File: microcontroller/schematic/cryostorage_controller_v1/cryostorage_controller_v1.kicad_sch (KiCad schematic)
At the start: 27 parts, among them J1 Screw_Terminal_01x04, J2 USB_A_Stacked, J3 Screw_Terminal_01x06, J4 Screw_Terminal_01x06, J5 Screw_Terminal_01x05, J6 Screw_Terminal_01x01, J7 Screw_Terminal_01x02, Q1 IRLB8721PBF, Q2 BSS138, Q3 IRLB8721PBF, Q4 IRLB8721PBF, Q5 BSS138, U1 Pico, U2 LT1086-3.3

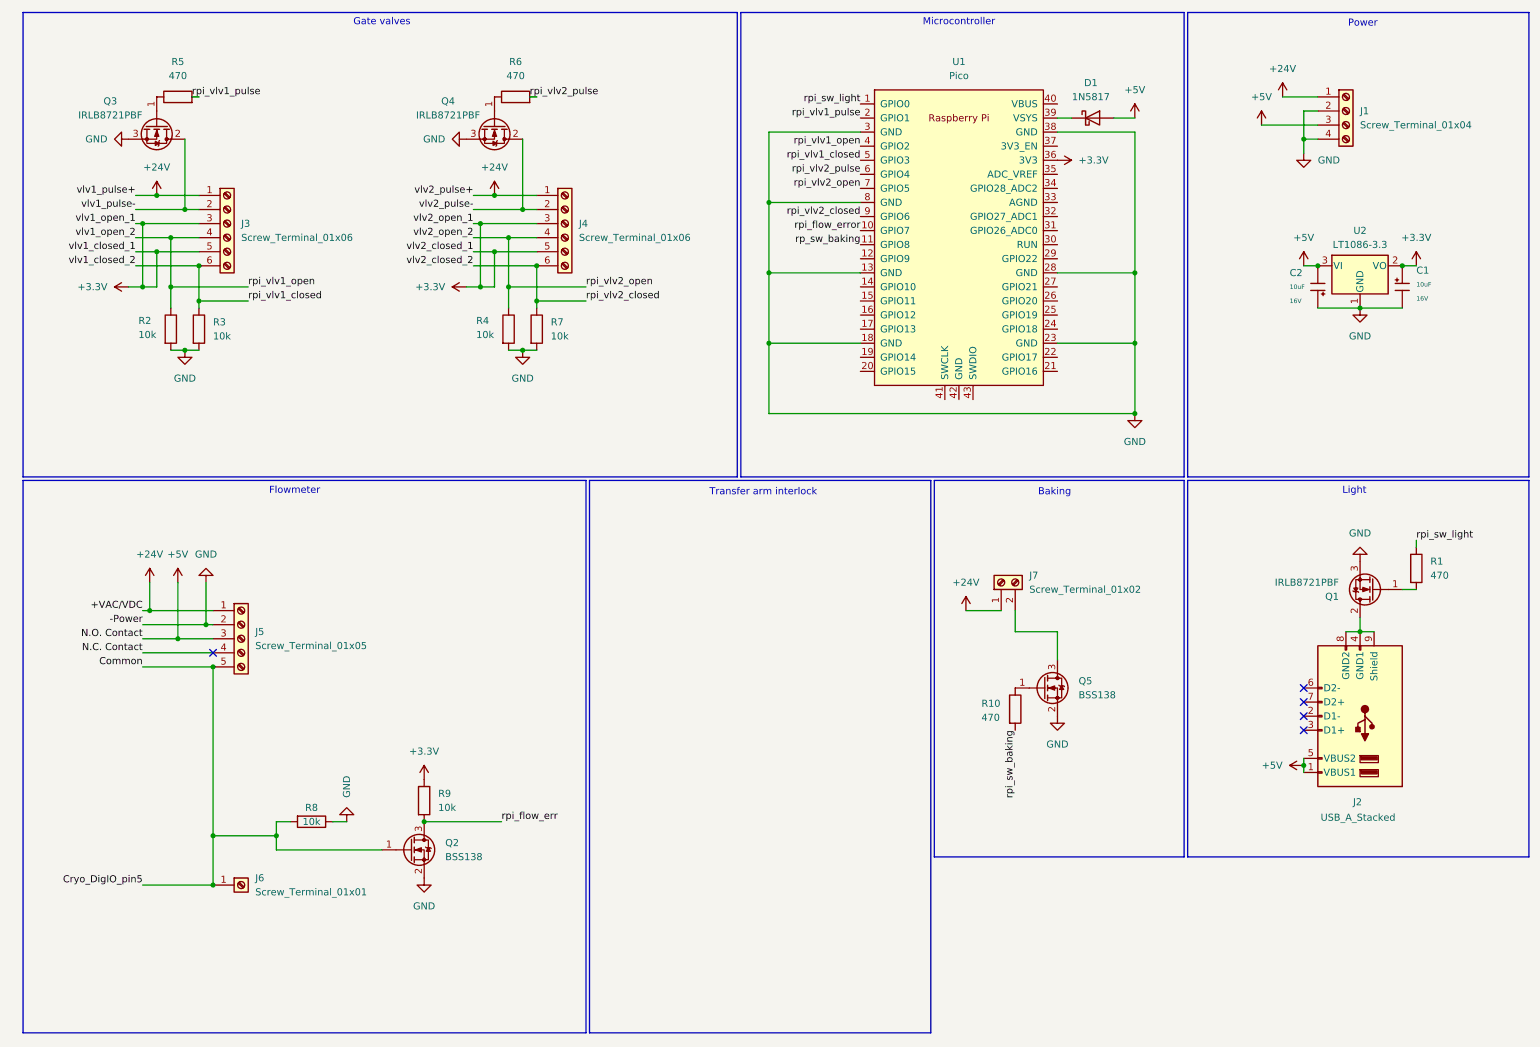
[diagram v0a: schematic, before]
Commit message: update schematic and add first PCB final version
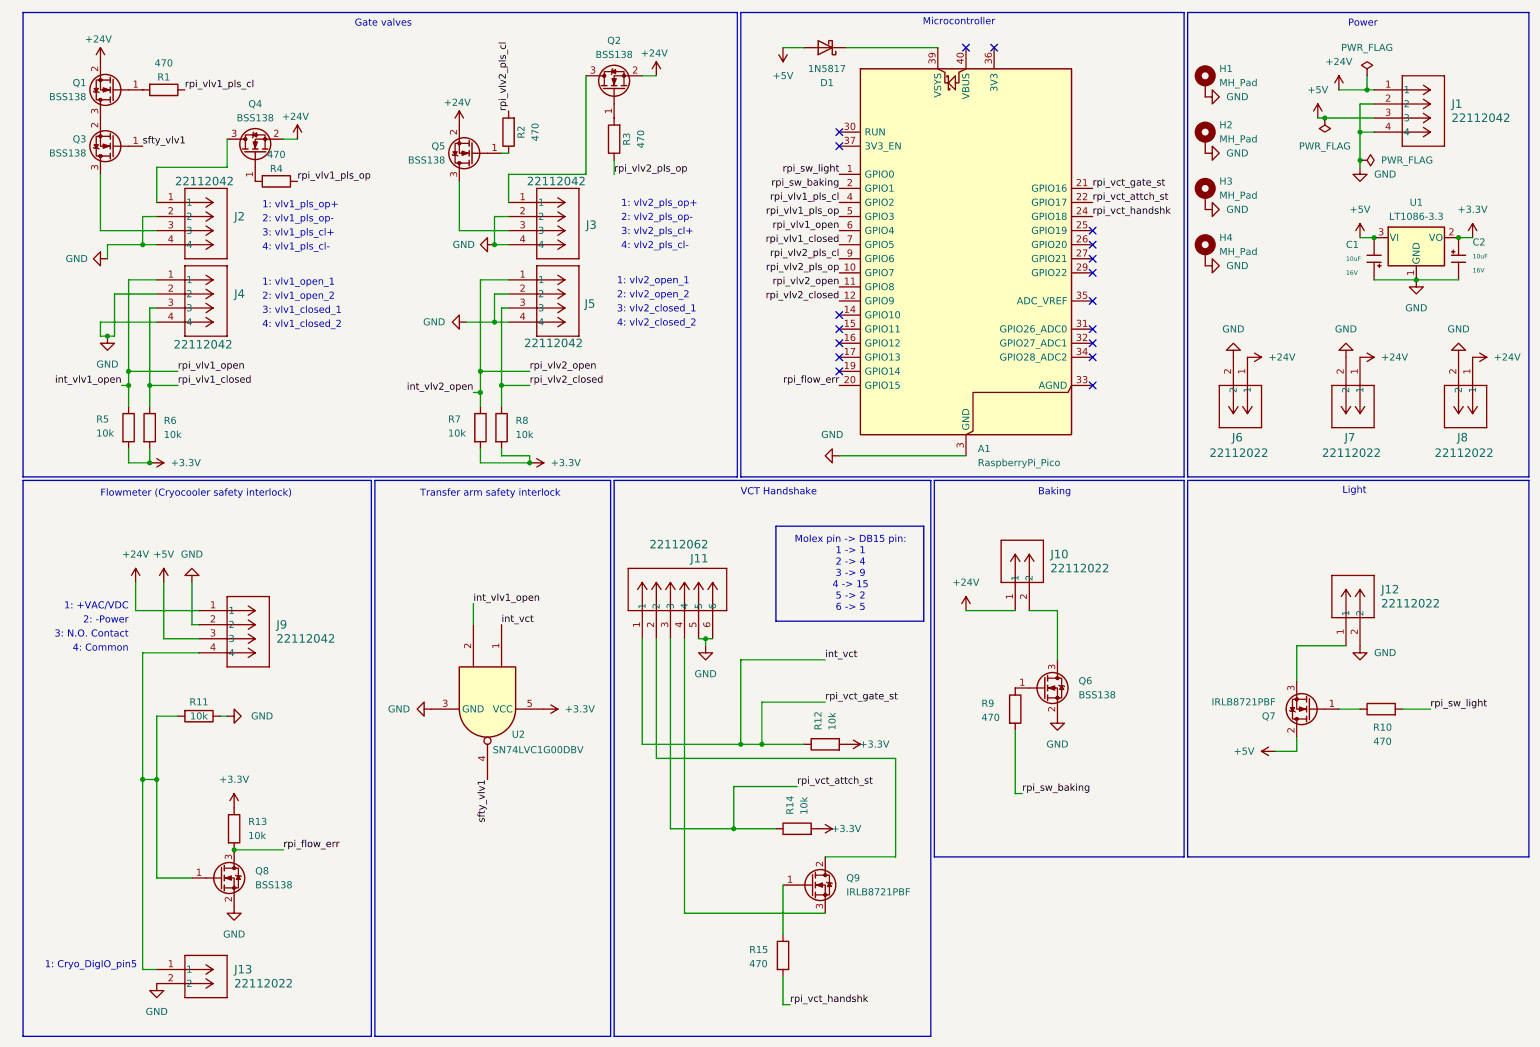
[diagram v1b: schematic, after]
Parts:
- removed J1: Screw_Terminal_01x04, symbol Connector:Screw_Terminal_01x04
- removed J2: USB_A_Stacked, symbol Connector:USB_A_Stacked
- removed J3, J4: Screw_Terminal_01x06, symbol Connector:Screw_Terminal_01x06
- removed J5: Screw_Terminal_01x05, symbol Connector:Screw_Terminal_01x05
- removed J6: Screw_Terminal_01x01, symbol Connector:Screw_Terminal_01x01
- removed J7: Screw_Terminal_01x02, symbol Connector:Screw_Terminal_01x02
- removed Q3, Q4: IRLB8721PBF, Package_TO_SOT_THT:TO-220-3_Vertical, symbol Transistor_FET:IRLB8721PBF
- removed U1: Pico, RPi_Pico:RPi_Pico_SMD_TH, symbol rpi:Pico
- added A1: RaspberryPi_Pico, Module:RaspberryPi_Pico_Common_THT, symbol MCU_Module:RaspberryPi_Pico
- added H1, H2, H3, H4: MH_Pad, MountingHole:MountingHole_3.2mm_M3_Pad, symbol Mechanical:MountingHole_Pad
- added J1, J2, J3, J4, J5, J9: 22112042, Snapeda:CONN_A-6373-04A_MOL, symbol Snapeda:22112042
- added J10, J12, J13, J6, J7, J8: 22112022, Snapeda:CONN_A-6373-02A_MOL, symbol Snapeda:22112022
- added J11: 22112062, Snapeda:CONN_A-6373-06A_MOL, symbol Snapeda:22112062
- added Q1, Q2, Q3, Q4, Q5: BSS138, Package_TO_SOT_SMD:SOT-23, symbol Transistor_FET:BSS138
- added Q9: IRLB8721PBF, Package_TO_SOT_THT:TO-220-3_Vertical, symbol Transistor_FET:IRLB8721PBF
- added R12, R14, R5, R8: 10k, Resistor_SMD:R_1206_3216Metric_Pad1.30x1.75mm_HandSolder, symbol Device:R
- added R15: 470, Resistor_SMD:R_1206_3216Metric_Pad1.30x1.75mm_HandSolder, symbol Device:R
- added U2: SN74LVC1G00DBV, Package_TO_SOT_SMD:SOT-23-5, symbol 74xGxx:SN74LVC1G00DBV
- R1: renamed from R5; footprint (none) -> Resistor_SMD:R_1206_3216Metric_Pad1.30x1.75mm_HandSolder
- R10: renamed from R1; footprint (none) -> Resistor_SMD:R_1206_3216Metric_Pad1.30x1.75mm_HandSolder
- R11: renamed from R8; footprint (none) -> Resistor_SMD:R_1206_3216Metric_Pad1.30x1.75mm_HandSolder
- R13: renamed from R9; footprint (none) -> Resistor_SMD:R_1206_3216Metric_Pad1.30x1.75mm_HandSolder
- R2, R3, R4: value 10k -> 470; footprint (none) -> Resistor_SMD:R_1206_3216Metric_Pad1.30x1.75mm_HandSolder
- R6: value 470 -> 10k; footprint (none) -> Resistor_SMD:R_1206_3216Metric_Pad1.30x1.75mm_HandSolder
- R7: footprint (none) -> Resistor_SMD:R_1206_3216Metric_Pad1.30x1.75mm_HandSolder
- R9: renamed from R10; footprint (none) -> Resistor_SMD:R_1206_3216Metric_Pad1.30x1.75mm_HandSolder
- U1: renamed from U2; footprint (none) -> Snapeda:TO220-3_T_LIT
- renumbered C2 to C1, C1 to C2, Q5 to Q6, Q1 to Q7, Q2 to Q8
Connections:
- net rpi_vlv2_pulse is gone; now on net +3.3V: R6.2
- net +24V: now also J1.1, J10.1, J6.1, J7.1, J8.1, J9.1, Q1.2 (S), Q2.2 (S), Q4.2 (S), Q5.2 (S)
- net +3.3V: now also R7.2, R12.2, R14.2, R5.2, R8.2, U2.5 (VCC)
- net +5V: now also Q7.2 (D), J1.3, J9.3
- net GND: now also A1.13 (GND), A1.18 (GND), A1.23 (GND), A1.28 (GND), A1.3 (GND), A1.38 (GND), A1.8 (GND), H1.1, H2.1, H3.1, H4.1, J1.2, J1.4, J11.5, J11.6, J12.2, J13.2, J2.2, J2.4, J3.2, J3.4, J4.2, J4.4, J5.2, J5.4, J6.2, J7.2, J8.2, J9.2, U2.3 (GND); no longer Q7.3 (S), R2.2, R3.2, R4.2, R7.2
- net rpi_flow_err: now also A1.20 (GPIO15)
- net rpi_sw_baking: now also A1.2 (GPIO1)
- net rpi_sw_light: now also R10.2, A1.1 (GPIO0); no longer R10.1
- net rpi_vlv1_closed: now also R6.1, A1.7 (GPIO5), J4.3; no longer R3.1
- net rpi_vlv2_closed: now also A1.12 (GPIO9), J5.3, R8.1; no longer R7.1
- net at D1.1 (K): now also A1.39 (VSYS)
- net rpi_vlv1_pls_cl: now reaches R1.1
- net rpi_vlv1_pls_cl: now also A1.4 (GPIO2)
- net at Q7.1 (G): now also R10.1; no longer R10.2
- net at Q6.3 (D): now also J10.2
- net Common: no longer names the net of Q8.1 (G), R11.2
- net Common: now also J13.1, J9.4
- net rpi_vlv1_open: no longer names the net of R2.1
- net rpi_vlv1_open: now also Q5.1 (G)
- net rpi_vlv1_pulse: no longer names the net of R1.2
- net rpi_vlv1_pulse: now also Q1.1 (G)
- net rpi_vlv2_open renamed rpi_vlv1_pls_op
- net rpi_vlv1_pls_op: now also A1.5 (GPIO3)
- new net: Q9.1 (G), R15.1
- new net: J11.2, Q9.2 (D)
- new net: J11.4, Q9.3 (S)
- new net: Q1.3 (D), Q3.2 (S)
- new net: J2.3, Q3.3 (D)
- new net: Q4.1 (G), R4.2
- new net: J2.1, Q4.3 (D)
- new net: J3.1, Q2.3 (D)
- new net: J3.3, Q5.3 (D)
- new net: J12.1, Q7.3 (S)
- new net: Q2.1 (G), R3.2
- new net int_vct: A1.21 (GPIO16), J11.1, R12.1, U2.1
- new net int_vlv1_open: A1.6 (GPIO4), J4.1, R5.1, U2.2
- new net int_vlv2_open: A1.11 (GPIO8), J5.1, R7.1
- new net rpi_vct_attch_st: A1.22 (GPIO17), J11.3, R14.1
- new net rpi_vct_handshk: A1.24 (GPIO18), R15.2
- new net rpi_vlv2_pls_cl: A1.9 (GPIO6), R2.2
- new net rpi_vlv2_pls_op: A1.10 (GPIO7), R3.1
- new net sfty_vlv1: Q3.1 (G), U2.4
- no-connect marks 5 -> 18
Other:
- note added: "1: +VAC/VDC"
- note added: "1: Cryo_DigIO_pin5"
- note added: "1: vlv1_open_1"
- note added: "1: vlv1_pls_op+"
- note added: "1: vlv2_open_1"
- note added: "1: vlv2_pls_op+"
- note added: "2: -Power"
- note added: "2: vlv1_open_2"
- note added: "2: vlv1_pls_op-"
- note added: "2: vlv2_open_2"
- note added: "2: vlv2_pls_op-"
- note added: "3: N.O. Contact"
- note added: "3: vlv1_closed_1"
- note added: "3: vlv1_pls_cl+"
- note added: "3: vlv2_closed_1"
- note added: "3: vlv2_pls_cl+"
- note added: "4: Common"
- note added: "4: vlv1_closed_2"
- note added: "4: vlv1_pls_cl-"
- note added: "4: vlv2_closed_2"
- note added: "4: vlv2_pls_cl-"
- note added: "Flowmeter (Cryocooler safety interlock)"
- note added: "Molex pin -> DB15 pin: 1 -> 1 2 -> 4 3 -> 9 4 -> 15 5 -> 2 6 -> 5"
- note added: "Transfer arm safety interlock"
- note added: "VCT Handshake"
- note removed: "Flowmeter"
- note removed: "Transfer arm interlock"
- moved on the sheet: C1, C2, D1, Q7, Q8, R1, R10, R11, R13, U1
